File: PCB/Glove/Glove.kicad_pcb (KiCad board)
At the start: 2 copper layers, 70 x 70 mm, 36 parts, among them J1 JST-PH-SM4-TB, J2 USB-C-Socket-V, J3 Wago, J4 Reset, J5 BTN, J7 TC2030-USB-NL-DS, Q1 CJ2301, Q3 CJ2301, U1 ESP32-S3-MINI-1, U3 TP4054, U4 ME6211C33M5G-N

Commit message: Tweak
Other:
- board text added: "3.7V LiPo"
- board text added: "5V"
- board text added: "TC2030"
- board text added: "U"

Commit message: Tidy
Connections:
- J7 pad 2: VBUS -> D-
- J7 pad 6: GND -> D-
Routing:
- net D-: track 43.7 -> 47.3 mm
- net VBUS: track 61.7 -> 64.9 mm
- net GND: track 95.0 -> 93.7 mm

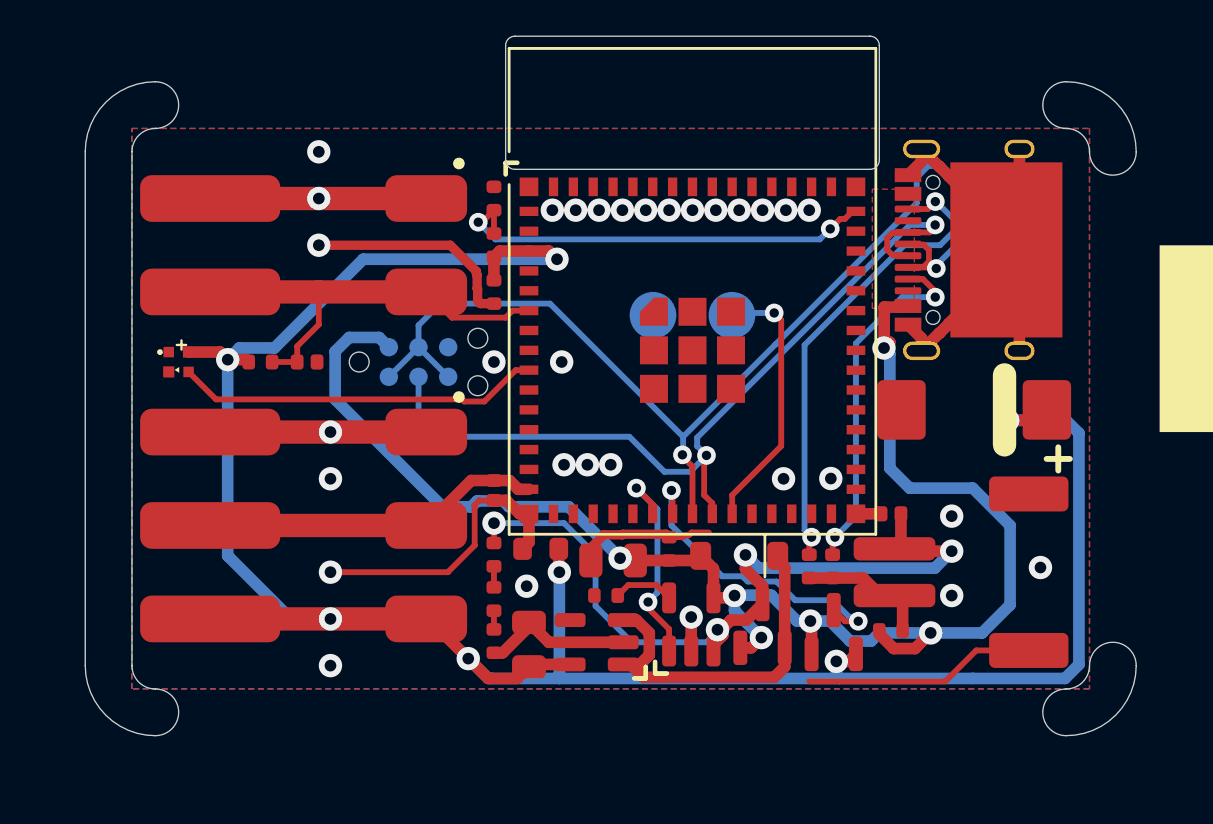
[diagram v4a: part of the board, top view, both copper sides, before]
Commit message: Added ADC and PWR
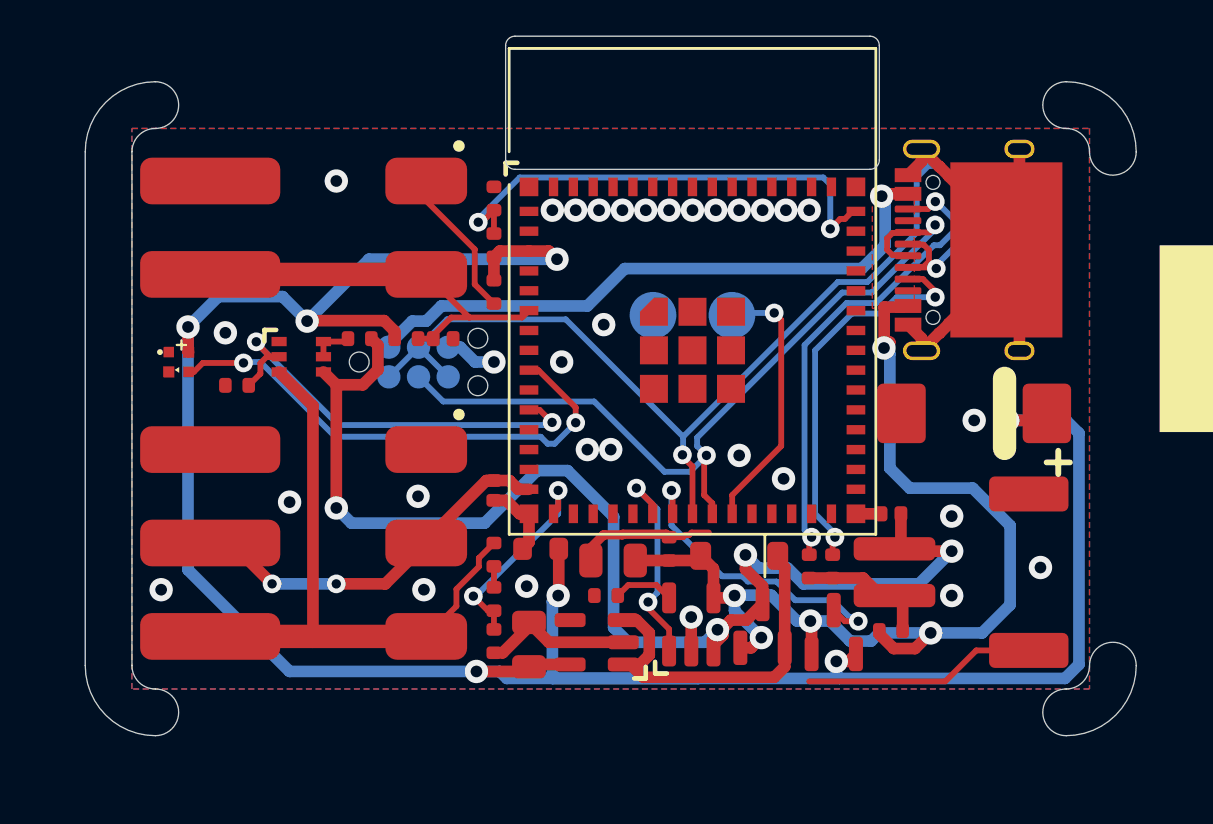
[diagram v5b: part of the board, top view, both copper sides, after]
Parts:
- added R15: 10K, RevK:R_0402, F.Cu at (84.5, 101.0)
- added R18: 10K, RevK:R_0402, F.Cu at (89.8, 99.0)
- added U5: NX6020CAKS, RevK:SOT-363_SC-70-6, F.Cu at (87.2, 99.8)
- moved R6 6.33 mm to (91.8, 99.0)
- moved D3 5.91 mm to (93.3, 99.0)
- moved J3 0.75 mm to (88.0, 107.8)
- moved J5 0.75 mm to (88.0, 94.2)
- moved C2 0.15 mm to (116.1, 102.2)
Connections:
- J3 pad 3: +3.3V -> VLED
- R9 pad 1: VBAT -> VLED
- U1 pad 11: unconnected-(U1-GPIO7-Pad11) -> PLED
- U1 pad 16: unconnected-(U1-GPIO12-Pad16) -> ADC1
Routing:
- net GND: track 93.7 -> 61.5 mm
- net VLED: track 0.00 -> 26.4 mm
- net VBAT: track 32.8 -> 52.4 mm
- net PLED: track 0.00 -> 18.8 mm, vias 0 -> 2
- net ADC1: track 0.80 -> 9.12 mm, vias 0 -> 2
- net +3.3V: track 101.9 -> 110.2 mm
- net RGB: track 15.7 -> 21.9 mm, vias 0 -> 2
- net VBUS: track 64.9 -> 70.5 mm
- net Net-(U1-EN): track 18.7 -> 21.1 mm
- net BTN: track 18.7 -> 17.1 mm
- net Net-(U5A-D): track 0.00 -> 1.58 mm
- net Net-(J2-CC1): track 15.3 -> 16.9 mm
- net D+: track 36.3 -> 35.5 mm
- net LED: vias 0 -> 2
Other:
- board text added: "3V7"
- board text added: "3V7 LiPo"
- board text added: "7 17 18 12"
- board text added: "PWR CHG USB ADC"
- board text removed: "17 18"
- board text removed: "3.7V LiPo"
- board text removed: "3V3"
- board text removed: "CHG USB"
